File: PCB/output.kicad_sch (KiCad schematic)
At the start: 8 parts, among them J2 Output Gate, Q1 BC547

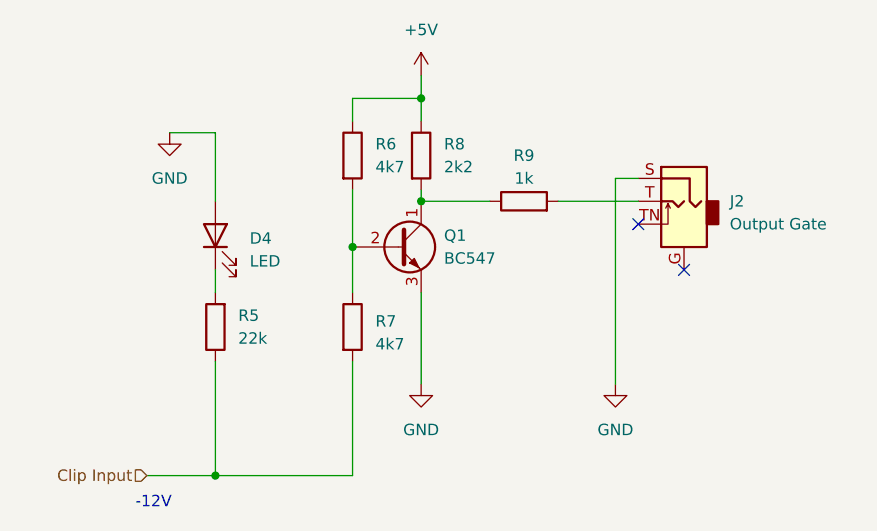
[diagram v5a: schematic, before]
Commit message: :art: Apply geographical reannotation
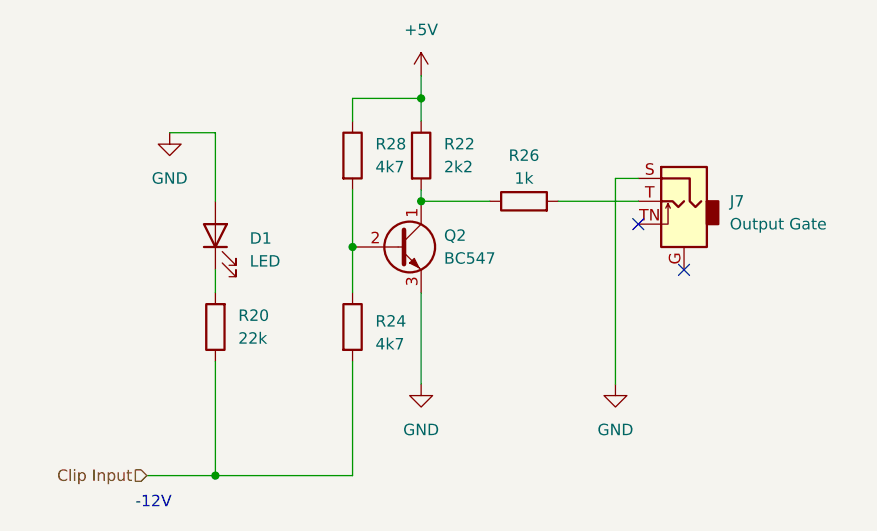
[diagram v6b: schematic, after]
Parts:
- renumbered D4 to D1, J2 to J7, Q1 to Q2, R5 to R20, R8 to R22, R7 to R24, R9 to R26, R6 to R28
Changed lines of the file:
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@@
   (symbol (lib_id "Device:LED") (at 137.16 86.36 90) (unit 1)
     (in_bom yes) (on_board yes) (dnp no) (fields_autoplaced)
-    (property "Reference" "D4" (at 140.97 86.6774 90)
+    (property "Reference" "D1" (at 140.97 86.6774 90)
       (effects (font (size 1.27 1.27)) (justify right))
     )
@@
       (project "misterclippy"
         (path "/e63e39d7-6ac0-4ffd-8aa3-1841a4541b55/28e15989-5385-427e-a9a7-25fddc57d8c9"
-          (reference "D4") (unit 1)
-        )
-        (path "/e63e39d7-6ac0-4ffd-8aa3-1841a4541b55/cb5a0e2d-897e-4b15-92a1-7875a38841f1"
-          (reference "D5") (unit 1)
+          (reference "D1") (unit 1)
+        )
+        (path "/e63e39d7-6ac0-4ffd-8aa3-1841a4541b55/cb5a0e2d-897e-4b15-92a1-7875a38841f1"
+          (reference "D2") (unit 1)
         )
       )
@@
   (symbol (lib_id "Device:R") (at 137.16 96.52 180) (unit 1)
     (in_bom yes) (on_board yes) (dnp no) (fields_autoplaced)
-    (property "Reference" "R5" (at 139.7 95.2499 0)
+    (property "Reference" "R20" (at 139.7 95.2499 0)
       (effects (font (size 1.27 1.27)) (justify right))
     )
@@
       (project "misterclippy"
         (path "/e63e39d7-6ac0-4ffd-8aa3-1841a4541b55/28e15989-5385-427e-a9a7-25fddc57d8c9"
-          (reference "R5") (unit 1)
-        )
-        (path "/e63e39d7-6ac0-4ffd-8aa3-1841a4541b55/cb5a0e2d-897e-4b15-92a1-7875a38841f1"
-          (reference "R10") (unit 1)
+          (reference "R20") (unit 1)
+        )
+        (path "/e63e39d7-6ac0-4ffd-8aa3-1841a4541b55/cb5a0e2d-897e-4b15-92a1-7875a38841f1"
+          (reference "R19") (unit 1)
         )
       )
@@
   (symbol (lib_id "Connector:AudioJack2_Ground_SwitchT") (at 189.23 82.55 0) (mirror y) (unit 1)
     (in_bom yes) (on_board yes) (dnp no) (fields_autoplaced)
-    (property "Reference" "J2" (at 194.31 82.55 0)
+    (property "Reference" "J7" (at 194.31 82.55 0)
       (effects (font (size 1.27 1.27)) (justify right))
     )
@@
       (project "misterclippy"
         (path "/e63e39d7-6ac0-4ffd-8aa3-1841a4541b55/28e15989-5385-427e-a9a7-25fddc57d8c9"
-          (reference "J2") (unit 1)
-        )
-        (path "/e63e39d7-6ac0-4ffd-8aa3-1841a4541b55/cb5a0e2d-897e-4b15-92a1-7875a38841f1"
-          (reference "J3") (unit 1)
+          (reference "J7") (unit 1)
+        )
+        (path "/e63e39d7-6ac0-4ffd-8aa3-1841a4541b55/cb5a0e2d-897e-4b15-92a1-7875a38841f1"
+          (reference "J8") (unit 1)
         )
       )
@@
   (symbol (lib_id "Device:R") (at 160.02 77.47 0) (unit 1)
     (in_bom yes) (on_board yes) (dnp no) (fields_autoplaced)
-    (property "Reference" "R8" (at 162.56 76.1999 0)
+    (property "Reference" "R22" (at 162.56 76.1999 0)
       (effects (font (size 1.27 1.27)) (justify left))
     )
@@
       (project "misterclippy"
         (path "/e63e39d7-6ac0-4ffd-8aa3-1841a4541b55/28e15989-5385-427e-a9a7-25fddc57d8c9"
-          (reference "R8") (unit 1)
-        )
-        (path "/e63e39d7-6ac0-4ffd-8aa3-1841a4541b55/cb5a0e2d-897e-4b15-92a1-7875a38841f1"
-          (reference "R13") (unit 1)
+          (reference "R22") (unit 1)
+        )
+        (path "/e63e39d7-6ac0-4ffd-8aa3-1841a4541b55/cb5a0e2d-897e-4b15-92a1-7875a38841f1"
+          (reference "R21") (unit 1)
         )
       )
@@
   (symbol (lib_id "Device:R") (at 152.4 96.52 0) (unit 1)
     (in_bom yes) (on_board yes) (dnp no) (fields_autoplaced)
-    (property "Reference" "R7" (at 154.94 95.885 0)
+    (property "Reference" "R24" (at 154.94 95.885 0)
       (effects (font (size 1.27 1.27)) (justify left))
     )
@@
       (project "misterclippy"
         (path "/e63e39d7-6ac0-4ffd-8aa3-1841a4541b55/28e15989-5385-427e-a9a7-25fddc57d8c9"
-          (reference "R7") (unit 1)
-        )
-        (path "/e63e39d7-6ac0-4ffd-8aa3-1841a4541b55/cb5a0e2d-897e-4b15-92a1-7875a38841f1"
-          (reference "R12") (unit 1)
+          (reference "R24") (unit 1)
+        )
+        (path "/e63e39d7-6ac0-4ffd-8aa3-1841a4541b55/cb5a0e2d-897e-4b15-92a1-7875a38841f1"
+          (reference "R23") (unit 1)
         )
       )
@@
   (symbol (lib_id "Device:R") (at 152.4 77.47 0) (unit 1)
     (in_bom yes) (on_board yes) (dnp no) (fields_autoplaced)
-    (property "Reference" "R6" (at 154.94 76.1999 0)
+    (property "Reference" "R28" (at 154.94 76.1999 0)
       (effects (font (size 1.27 1.27)) (justify left))
     )
@@
       (project "misterclippy"
         (path "/e63e39d7-6ac0-4ffd-8aa3-1841a4541b55/28e15989-5385-427e-a9a7-25fddc57d8c9"
-          (reference "R6") (unit 1)
-        )
-        (path "/e63e39d7-6ac0-4ffd-8aa3-1841a4541b55/cb5a0e2d-897e-4b15-92a1-7875a38841f1"
-          (reference "R11") (unit 1)
+          (reference "R28") (unit 1)
+        )
+        (path "/e63e39d7-6ac0-4ffd-8aa3-1841a4541b55/cb5a0e2d-897e-4b15-92a1-7875a38841f1"
+          (reference "R27") (unit 1)
         )
       )
@@
   (symbol (lib_id "Device:R") (at 171.45 82.55 90) (unit 1)
     (in_bom yes) (on_board yes) (dnp no) (fields_autoplaced)
-    (property "Reference" "R9" (at 171.45 77.47 90)
+    (property "Reference" "R26" (at 171.45 77.47 90)
       (effects (font (size 1.27 1.27)))
     )
@@
       (project "misterclippy"
         (path "/e63e39d7-6ac0-4ffd-8aa3-1841a4541b55/28e15989-5385-427e-a9a7-25fddc57d8c9"
-          (reference "R9") (unit 1)
-        )
-        (path "/e63e39d7-6ac0-4ffd-8aa3-1841a4541b55/cb5a0e2d-897e-4b15-92a1-7875a38841f1"
-          (reference "R14") (unit 1)
+          (reference "R26") (unit 1)
+        )
+        (path "/e63e39d7-6ac0-4ffd-8aa3-1841a4541b55/cb5a0e2d-897e-4b15-92a1-7875a38841f1"
+          (reference "R25") (unit 1)
         )
       )
@@
   (symbol (lib_id "Transistor_BJT:BC547") (at 157.48 87.63 0) (unit 1)
     (in_bom yes) (on_board yes) (dnp no) (fields_autoplaced)
-    (property "Reference" "Q1" (at 162.56 86.3599 0)
+    (property "Reference" "Q2" (at 162.56 86.3599 0)
       (effects (font (size 1.27 1.27)) (justify left))
     )
@@
       (project "misterclippy"
         (path "/e63e39d7-6ac0-4ffd-8aa3-1841a4541b55/28e15989-5385-427e-a9a7-25fddc57d8c9"
+          (reference "Q2") (unit 1)
+        )
+        (path "/e63e39d7-6ac0-4ffd-8aa3-1841a4541b55/cb5a0e2d-897e-4b15-92a1-7875a38841f1"
           (reference "Q1") (unit 1)
         )
-        (path "/e63e39d7-6ac0-4ffd-8aa3-1841a4541b55/cb5a0e2d-897e-4b15-92a1-7875a38841f1"
-          (reference "Q2") (unit 1)
-        )
-      )
+      )

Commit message: :art: Change transistor footprint for hand soldering
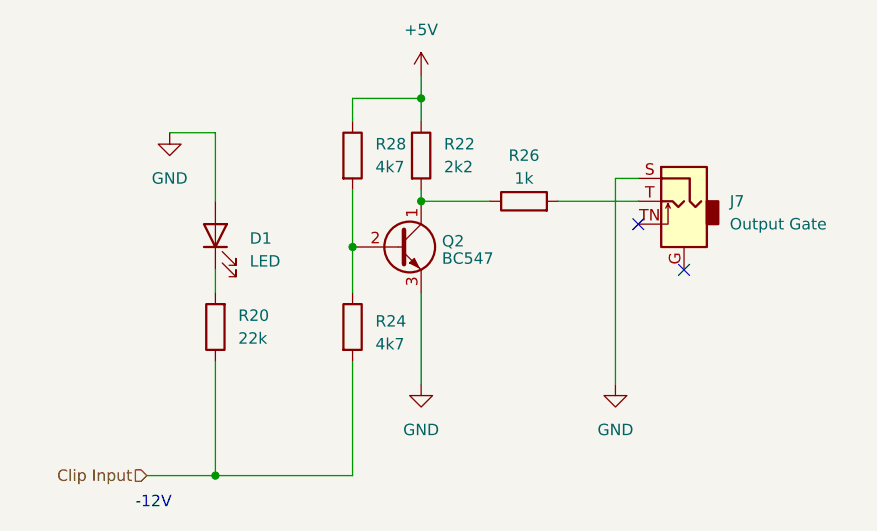
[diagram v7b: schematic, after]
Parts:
- Q2: footprint Package_TO_SOT_THT:TO-92_Inline -> Package_TO_SOT_THT:TO-92_HandSolder
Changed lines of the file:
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@@
   (symbol (lib_id "Transistor_BJT:BC547") (at 157.48 87.63 0) (unit 1)
     (in_bom yes) (on_board yes) (dnp no) (fields_autoplaced)
-    (property "Reference" "Q2" (at 162.56 86.3599 0)
+    (property "Reference" "Q2" (at 162.3314 86.9863 0)
       (effects (font (size 1.27 1.27)) (justify left))
     )
-    (property "Value" "BC547" (at 162.56 88.8999 0)
+    (property "Value" "BC547" (at 162.3314 88.9073 0)
       (effects (font (size 1.27 1.27)) (justify left))
     )
-    (property "Footprint" "Package_TO_SOT_THT:TO-92_Inline" (at 162.56 89.535 0)
+    (property "Footprint" "Package_TO_SOT_THT:TO-92_HandSolder" (at 162.56 89.535 0)
       (effects (font (size 1.27 1.27) italic) (justify left) hide)
     )
